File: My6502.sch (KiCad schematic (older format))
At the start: 28 parts, among them J1 IRQ_SEL, J2 CLK Jumper, J3 Barrel_Jack_Switch, J5 IRQ_Pullup, SW1 SW_Push_Dual, U1 28C256, U2 WD65C02, U3 CY62256-70PC, U4 74HCT00, U5 74HCT02, U6 DS1813-10, U7 74LS21, X1 CXO_DIP14

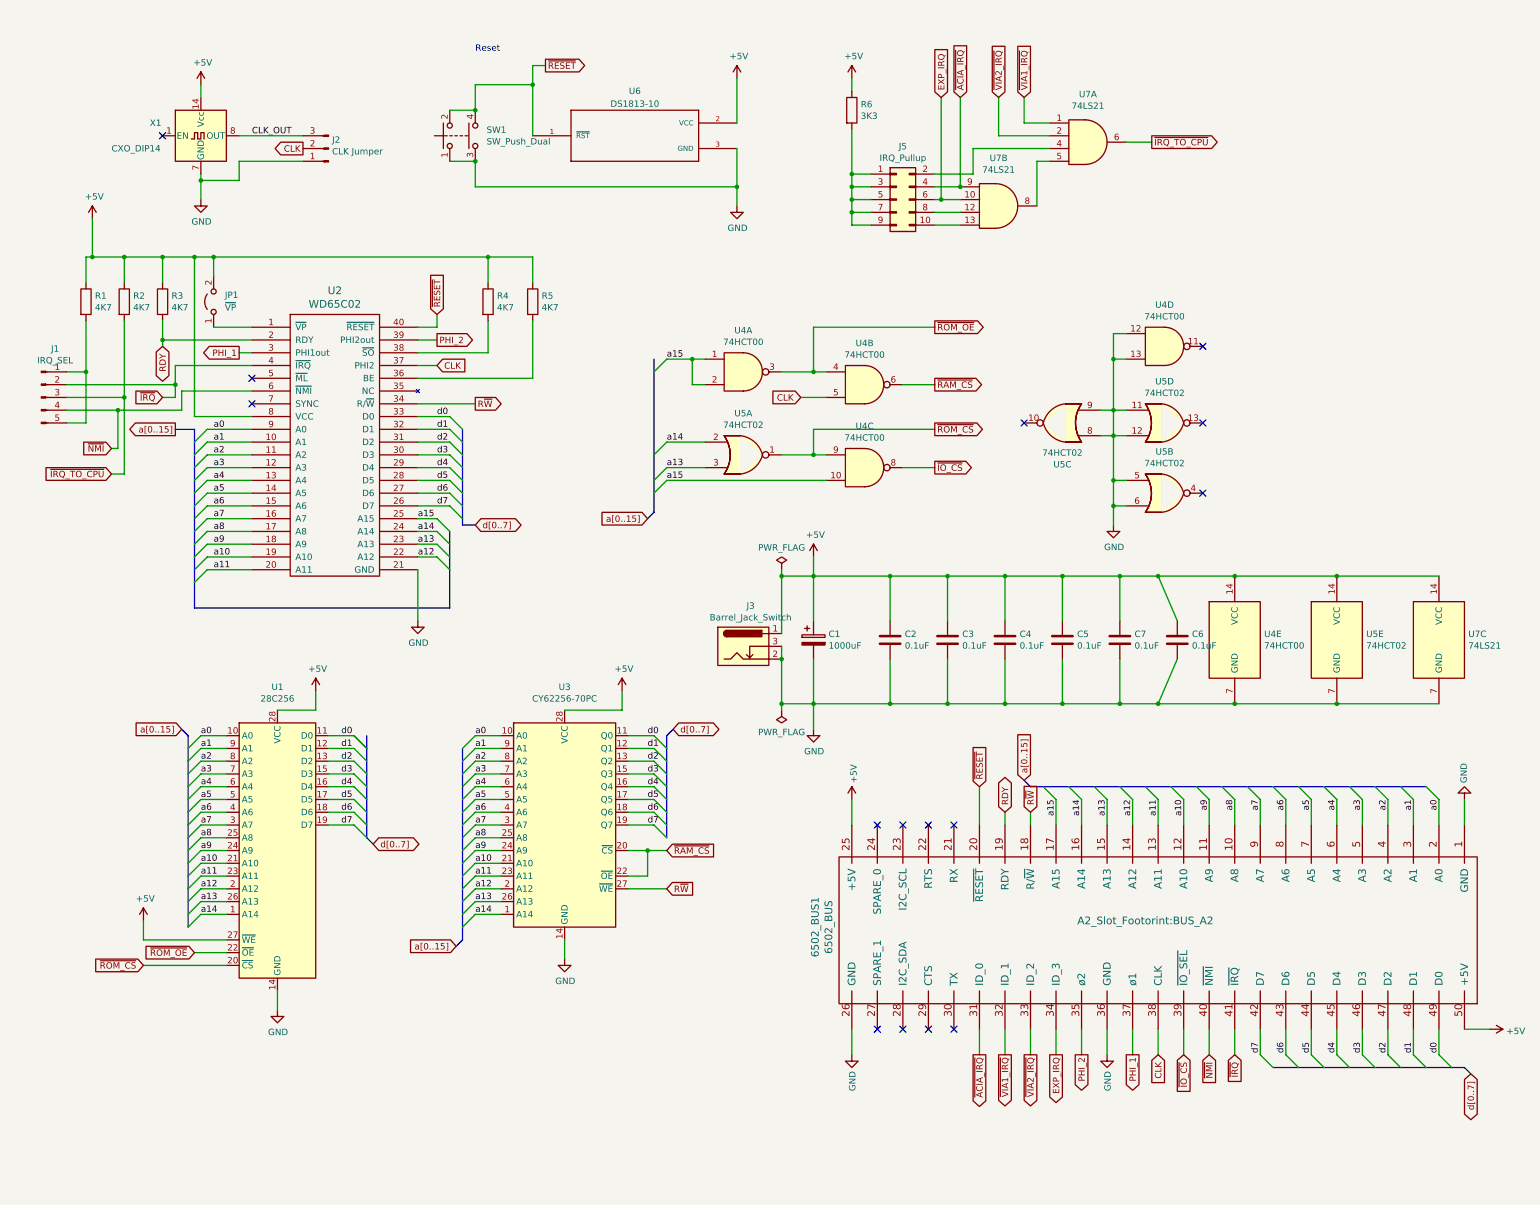
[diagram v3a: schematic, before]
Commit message: Clean processor board schematic
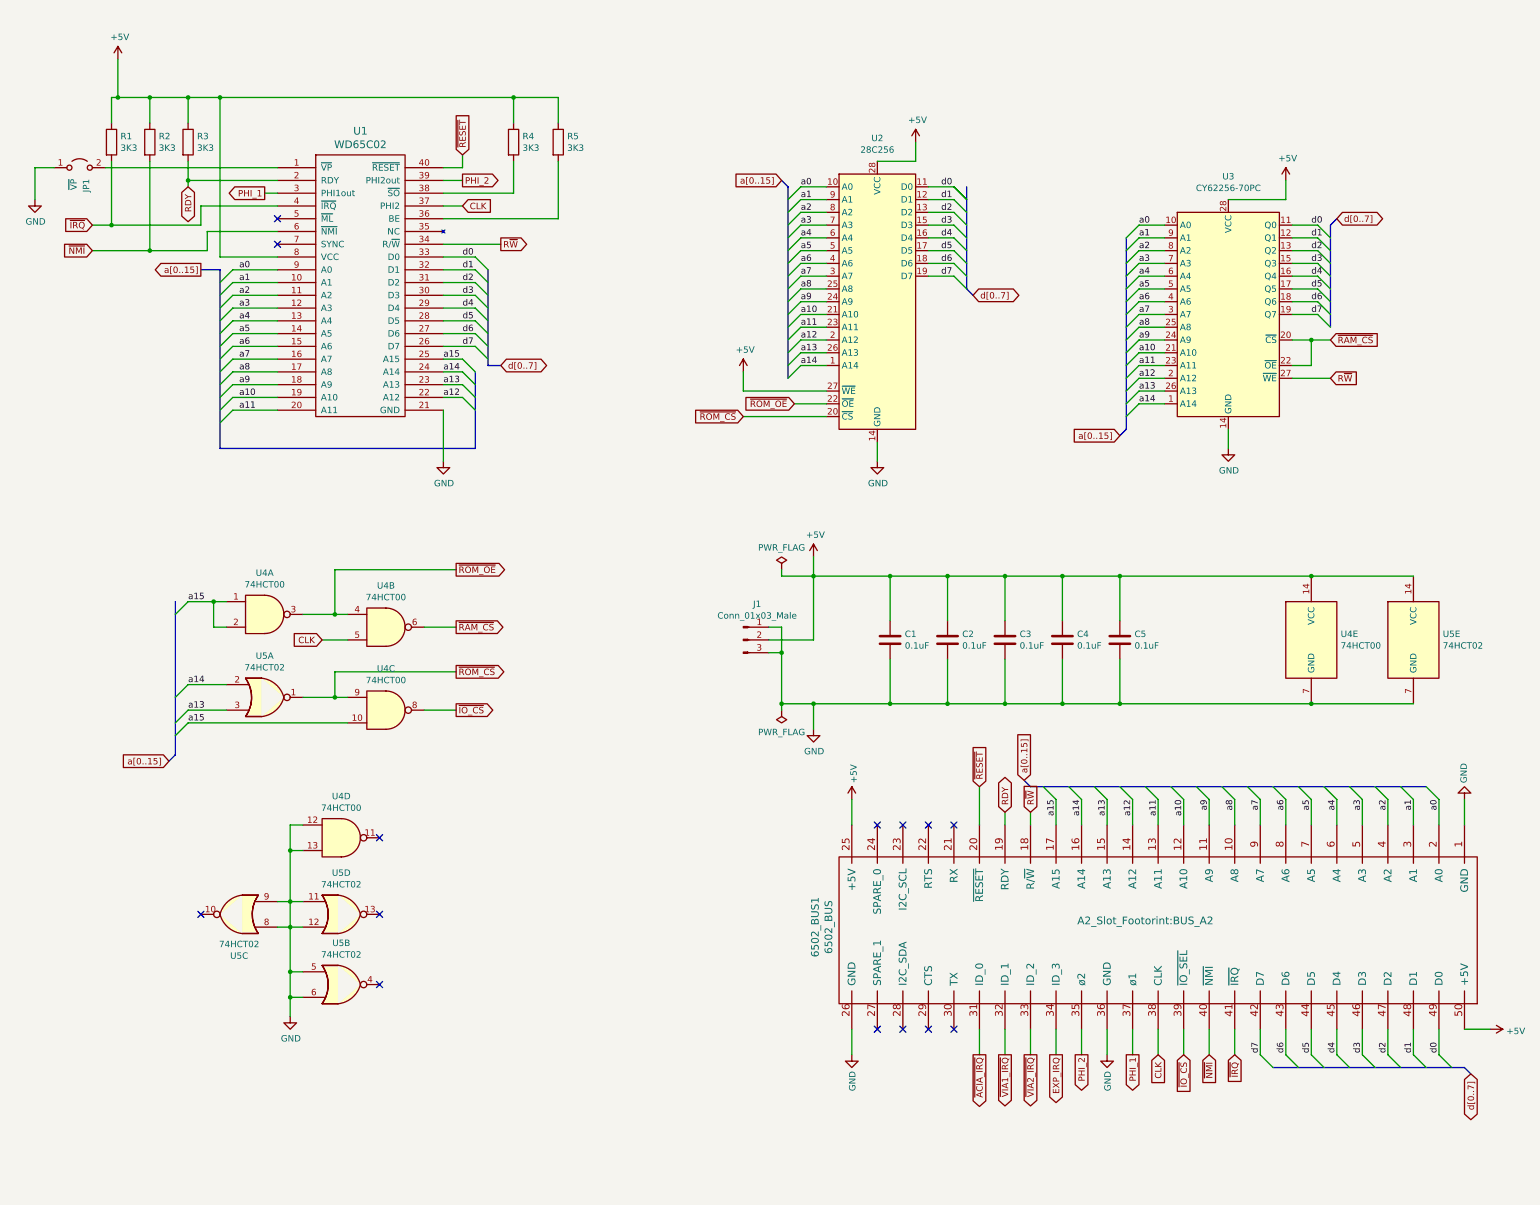
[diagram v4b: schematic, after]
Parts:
- removed C1: 1000uF, Capacitor_THT:CP_Radial_D8.0mm_P3.80mm, symbol Device:CP
- removed C6: 0.1uF, Capacitor_THT:C_Disc_D4.3mm_W1.9mm_P5.00mm, symbol Device:C
- removed J1: IRQ_SEL, Connector_PinHeader_2.54mm:PinHeader_1x05_P2.54mm_Vertical, symbol Connector:Conn_01x05_Male
- removed J2: CLK Jumper, Connector_PinHeader_2.54mm:PinHeader_1x03_P2.54mm_Vertical, symbol Connector:Conn_01x03_Male
- removed J3: Barrel_Jack_Switch, Connector_BarrelJack:BarrelJack_Horizontal, symbol Connector:Barrel_Jack_Switch
- removed J5: IRQ_Pullup, Connector_PinHeader_2.54mm:PinHeader_2x05_P2.54mm_Vertical, symbol Connector_Generic:Conn_02x05_Odd_Even
- removed R6: 3K3, Resistor_THT:R_Axial_DIN0207_L6.3mm_D2.5mm_P10.16mm_Horizontal, symbol Device:R
- removed SW1: SW_Push_Dual, Button_Switch_THT:SW_TH_Tactile_Omron_B3F-10xx, symbol Switch:SW_Push_Dual
- removed U6: DS1813-10, Package_TO_SOT_THT:TO-92, symbol DS1813-10:DS1813-10
- removed U7: 74LS21, Package_DIP:DIP-14_W7.62mm_Socket_LongPads, symbol 74xx:74LS21
- removed X1: CXO_DIP14, Oscillator:Oscillator_DIP-14, symbol Oscillator:CXO_DIP14
- added J1: Conn_01x03_Male, Connector_PinSocket_2.54mm:PinSocket_1x03_P2.54mm_Vertical, symbol Connector:Conn_01x03_Male
- R1, R2, R3, R4, R5: value 4K7 -> 3K3
- renumbered C2 to C1, C3 to C2, C4 to C3, C5 to C4, C7 to C5, U2 to U1, U1 to U2
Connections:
- net ~IRQ_TO_CPU is gone; now on net ~NMI: R2.2
- net +5V: now also J1.2 (Pin_2); no longer JP1.2 (B)
- net GND: now also JP1.1 (A), J1.1 (Pin_1), J1.3 (Pin_3)
- net ~IRQ: now also R1.2
- net at U1.1 (~VP): now also JP1.2 (B); no longer JP1.1 (A)
- no-connect marks 15 -> 14
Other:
- note removed: "Reset"
- moved on the sheet: JP1, R1, R2, R3, R4, R5, U1, U2, U3, U4A, U4B, U4C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

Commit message: Rev 1 with silkscreen
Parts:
- J1: value Conn_01x03_Male -> POWER
- U1: value WD65C02 -> CPU - WD65C02
- U2: value 28C256 -> ROM - 28C256
- U3: value CY62256-70PC -> RAM - 62256
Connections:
- net EXP_IRQ: no longer names the net of 6502_BUS1.34 (ID_3)
- net ~ACIA_IRQ: no longer names the net of 6502_BUS1.31 (ID_0)
- net ~VIA1_IRQ: no longer names the net of 6502_BUS1.32 (ID_1)
- net ~VIA2_IRQ: no longer names the net of 6502_BUS1.33 (ID_2)
- no-connect marks 14 -> 18
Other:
- note added: "- 32k bytes of RAM (address range $0000-$7FFF) \n- 8k bytes if I/O ($8000-$9FFF).\n- 24k bytes ROM ($A000-$FFFF)"
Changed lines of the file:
@@
 P 2650 2000
 F 0 "U1" H 2650 3187 60  0000 C CNN
-F 1 "WD65C02" H 2650 3081 60  0000 C CNN
+F 1 "CPU - WD65C02" H 2650 3081 60  0000 C CNN
 F 2 "Package_DIP:DIP-40_W15.24mm_Socket_LongPads" H 2150 2200 60  0001 C CNN
 F 3 "" H 2150 2200 60  0000 C CNN
@@
 Wire Wire Line
 	2450 4600 2550 4600
-Text GLabel 2350 4800 0    50   Input ~ 0
-CLK
 Wire Wire Line
 	2350 4800 2550 4800
@@
 P 9450 2250
 F 0 "U3" H 9450 3331 50  0000 C CNN
-F 1 "CY62256-70PC" H 9450 3240 50  0000 C CNN
+F 1 "RAM - 62256" H 9450 3240 50  0000 C CNN
 F 2 "Package_DIP:DIP-28_W15.24mm_Socket_LongPads" H 9450 2150 50  0001 C CNN
 F 3 "https://ecee.colorado.edu/~mcclurel/Cypress_SRAM_CY62256.pdf" H 9450 2150 50  0001 C CNN
@@
 P 6700 2150
 F 0 "U2" H 6700 3431 50  0000 C CNN
-F 1 "28C256" H 6700 3340 50  0000 C CNN
+F 1 "ROM - 28C256" H 6700 3340 50  0000 C CNN
 F 2 "Package_DIP:DIP-28_W15.24mm_Socket_LongPads" H 6700 2150 50  0001 C CNN
 F 3 "http://ww1.microchip.com/downloads/en/DeviceDoc/doc0006.pdf" H 6700 2150 50  0001 C CNN
@@
 Wire Bus Line
 	11300 8150 11350 8200
-Text GLabel 8900 8050 3    50   Input ~ 0
+Text GLabel 8900 8050 3    50   Output ~ 0
 CLK
 Text GLabel 7900 6150 1    50   Input ~ 0
@@
 Text GLabel 7500 5950 1    50   Input ~ 0
 ~RESET
-Text GLabel 8100 8050 3    50   Output ~ 0
-EXP_IRQ
 Wire Wire Line
 	7900 6250 7900 6150
@@
 Wire Wire Line
 	6500 6250 6500 6050
-Text GLabel 7500 8050 3    50   Output ~ 0
-~ACIA_IRQ
-Text GLabel 7700 8050 3    50   Output ~ 0
-~VIA1_IRQ
-Text GLabel 7900 8050 3    50   Output ~ 0
-~VIA2_IRQ
 $Comp
 L Device:C C5
@@
 	9500 8050 9500 7850
 Wire Wire Line
-	7500 8050 7500 7850
-Wire Wire Line
-	7700 8050 7700 7850
-Wire Wire Line
-	7900 8050 7900 7850
-Wire Wire Line
-	8100 8050 8100 7850
-Wire Wire Line
 	700  1050 700  1550
 Connection ~ 700  1550
@@
 P 5650 4800
 F 0 "J1" H 5758 5081 50  0000 C CNN
-F 1 "Conn_01x03_Male" H 5758 4990 50  0000 C CNN
+F 1 "POWER" H 5758 4990 50  0000 C CNN
 F 2 "Connector_PinSocket_2.54mm:PinSocket_1x03_P2.54mm_Vertical" H 5650 4800 50  0001 C CNN
 F 3 "~" H 5650 4800 50  0001 C CNN
@@
 Wire Wire Line
 	6200 4800 6200 4300
+NoConn ~ 7500 7850
+NoConn ~ 7700 7850
+NoConn ~ 7900 7850
+NoConn ~ 8100 7850
+Text GLabel 2350 4800 0    50   Input ~ 0
+CLK
 Wire Bus Line
 	1200 4500 1200 5700
@@
 Wire Bus Line
 	7900 5950 11000 5950
+Text Notes 3300 5900 0    50   ~ 0
+- 32k bytes of RAM (address range $0000-$7FFF) \n- 8k bytes if  I/O ($8000-$9FFF).\n- 24k bytes ROM ($A000-$FFFF)
 $EndSCHEMATC
